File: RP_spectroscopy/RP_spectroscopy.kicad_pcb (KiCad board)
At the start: 2 copper layers, 90.5 x 109 mm, 79 parts, among them J1 Extension connector 1, J10 Conn_Coaxial, J2 Extension connector 2, J3 Conn_Coaxial, J4 Conn_Coaxial, J5 Conn_Coaxial, J6 Conn_Coaxial, J7 Molex PicoBlade, J8 Molex PicoBlade, J9 Conn_Coaxial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

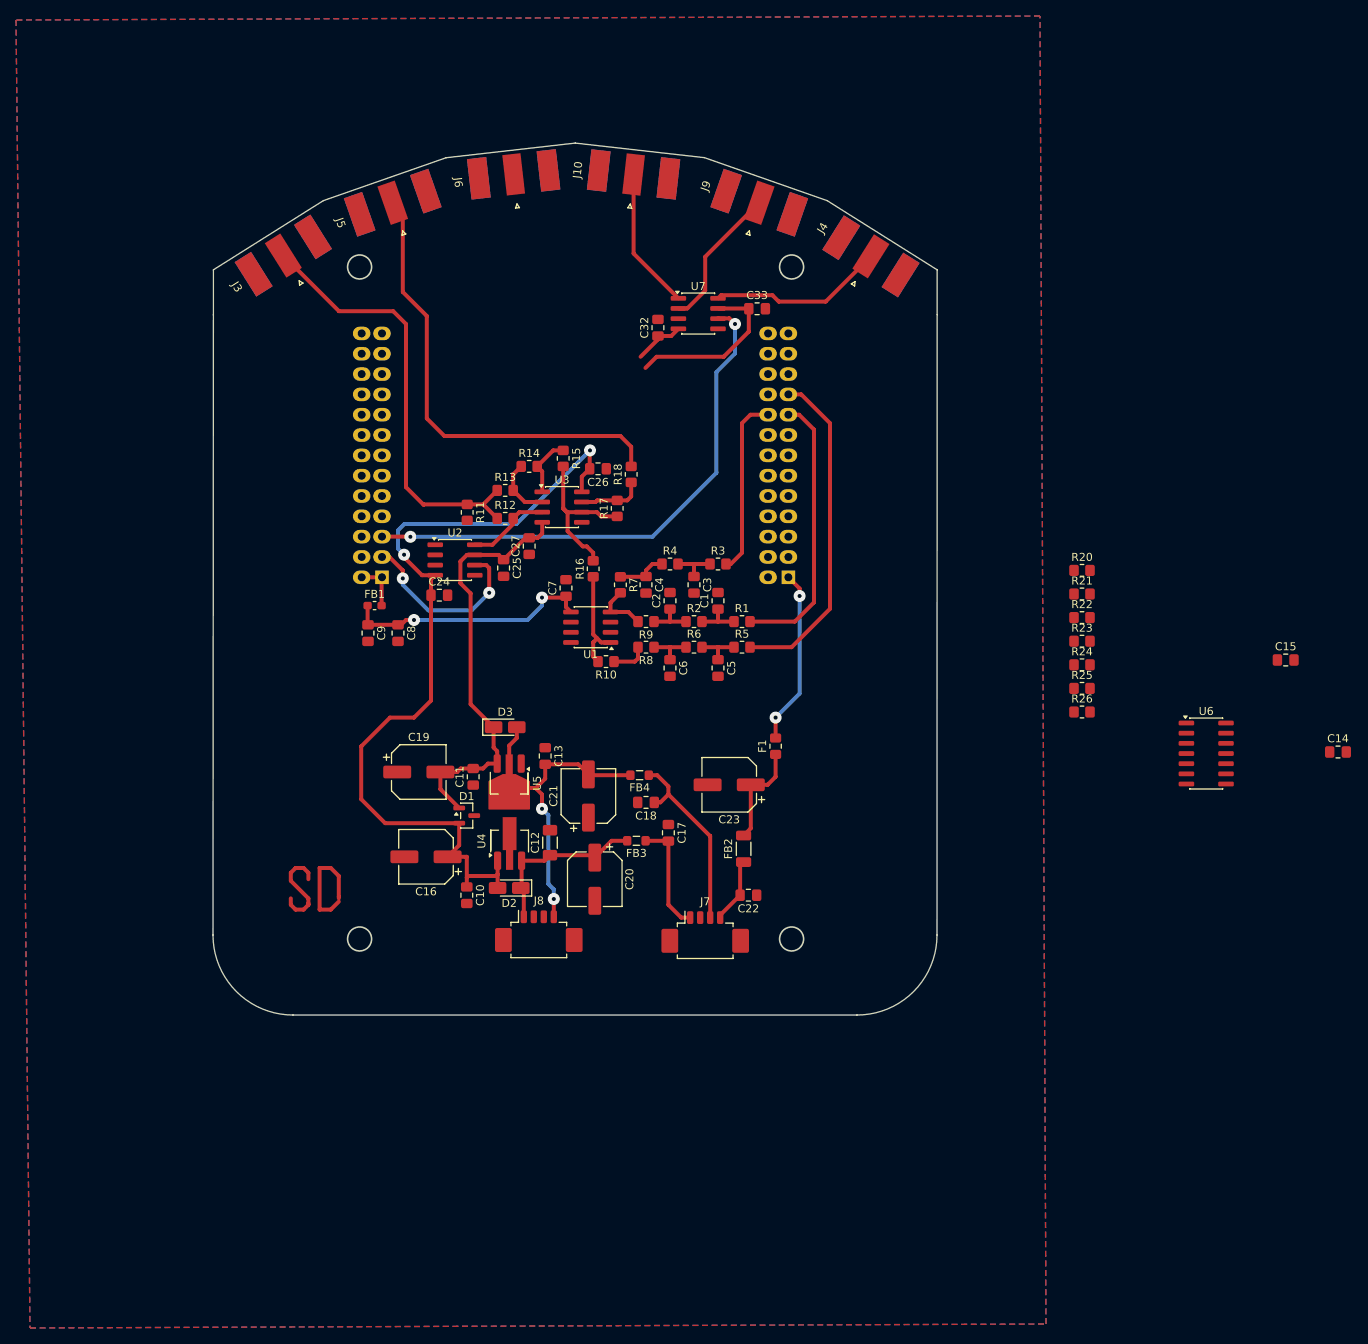
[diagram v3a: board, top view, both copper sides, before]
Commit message: Added the BP filter and the amplification stages. It should be done.
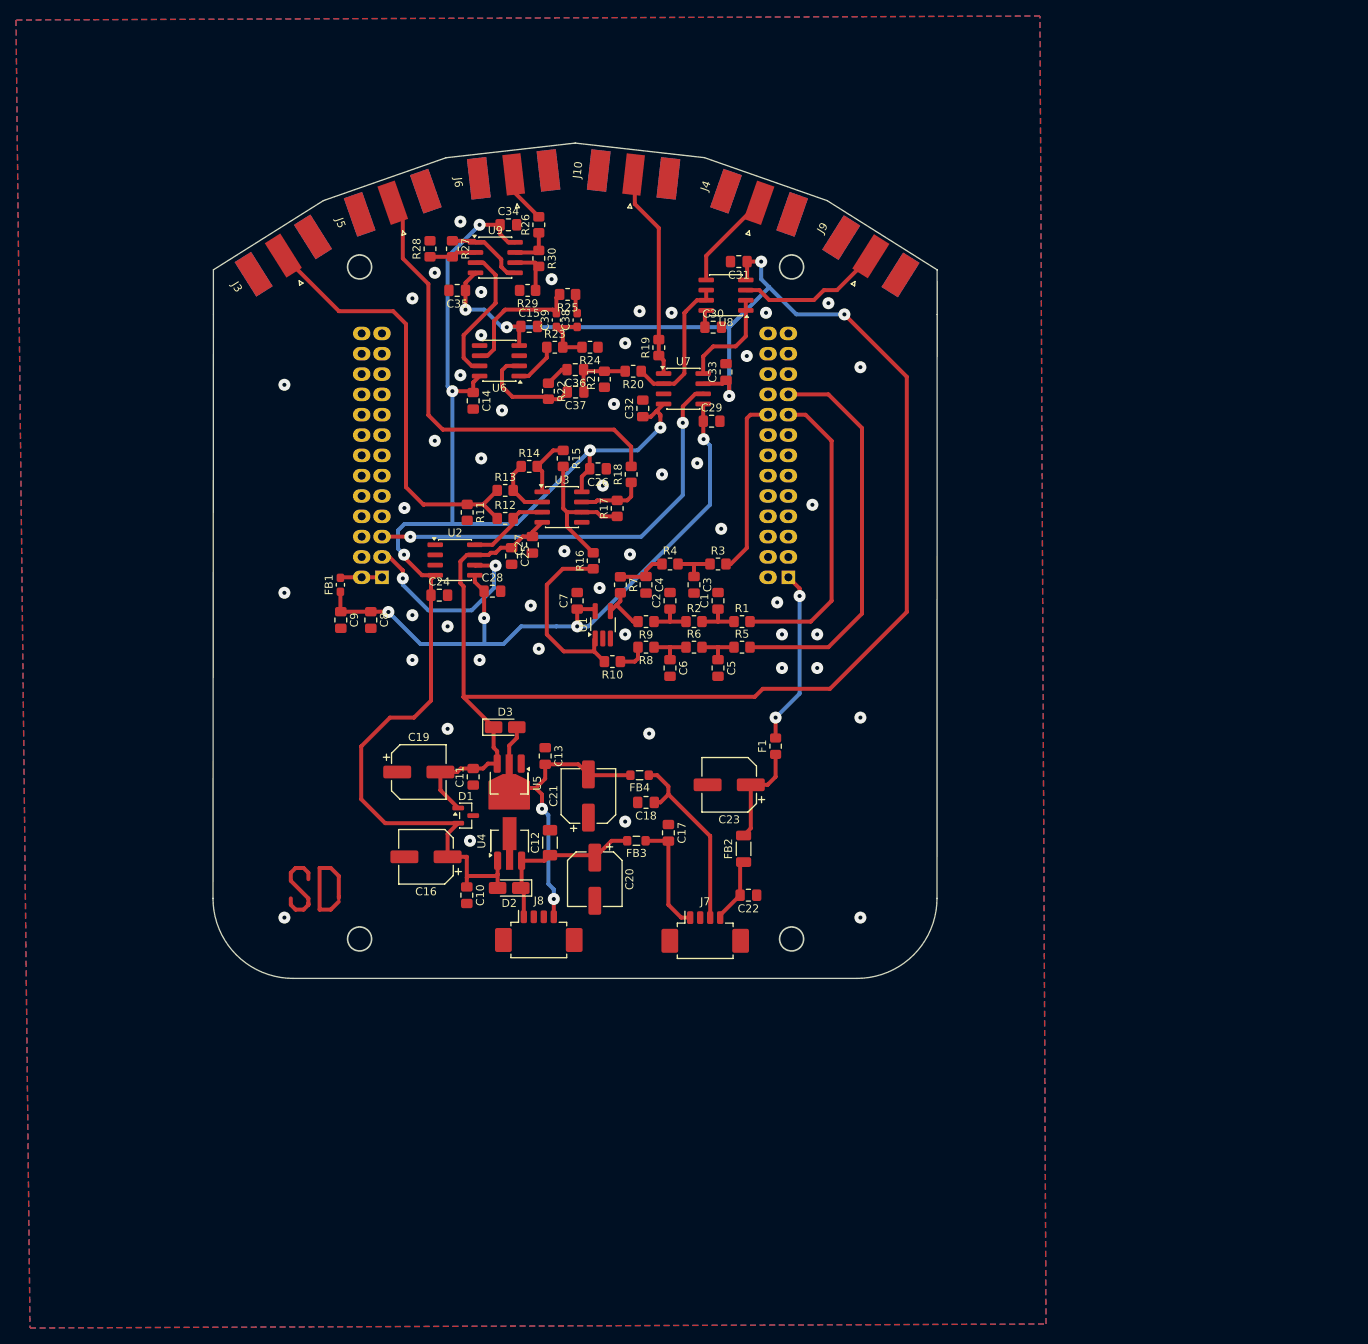
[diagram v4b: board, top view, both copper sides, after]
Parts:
- added C28: 100n, Capacitor_SMD:C_0805_2012Metric_Pad1.18x1.45mm_HandSolder, F.Cu at (124.8, 89.4)
- added C29: 100n, Capacitor_SMD:C_0805_2012Metric_Pad1.18x1.45mm_HandSolder, F.Cu at (152.2, 68.2)
- added C30: 100n, Capacitor_SMD:C_0805_2012Metric_Pad1.18x1.45mm_HandSolder, F.Cu at (152.4, 56.4)
- added C31: 100n, Capacitor_SMD:C_0805_2012Metric_Pad1.18x1.45mm_HandSolder, F.Cu at (155.6, 48.2)
- added C34: 100n, Capacitor_SMD:C_0805_2012Metric_Pad1.18x1.45mm_HandSolder, F.Cu at (126.8, 43.6)
- added C35: 100n, Capacitor_SMD:C_0805_2012Metric_Pad1.18x1.45mm_HandSolder, F.Cu at (120.4, 51.8)
- added C36: 4.3nF, Capacitor_SMD:C_0805_2012Metric_Pad1.18x1.45mm_HandSolder, F.Cu at (135.2, 61.7)
- added C37: 4.3nF, Capacitor_SMD:C_0805_2012Metric_Pad1.18x1.45mm_HandSolder, F.Cu at (135.2, 64.5)
- added C38: 2.4nF, Capacitor_SMD:C_0603_1608Metric_Pad1.08x0.95mm_HandSolder, F.Cu at (135.4, 55.5)
- added C39: 2.4nF, Capacitor_SMD:C_0603_1608Metric_Pad1.08x0.95mm_HandSolder, F.Cu at (132.8, 55.5)
- added R19: 49R9, Resistor_SMD:R_0805_2012Metric_Pad1.20x1.40mm_HandSolder, F.Cu at (145.6, 59.0)
- added R27: R, Resistor_SMD:R_0805_2012Metric_Pad1.20x1.40mm_HandSolder, F.Cu at (119.8, 46.6)
- added R28: R, Resistor_SMD:R_0805_2012Metric_Pad1.20x1.40mm_HandSolder, F.Cu at (117.0, 46.6)
- added R29: R, Resistor_SMD:R_0805_2012Metric_Pad1.20x1.40mm_HandSolder, F.Cu at (129.2, 51.8)
- added R30: R, Resistor_SMD:R_0805_2012Metric_Pad1.20x1.40mm_HandSolder, F.Cu at (130.6, 47.8)
- added U8: LT6231, Package_SO:SOIC-8_3.9x4.9mm_P1.27mm, F.Cu at (154.0, 52.4)
- added U9: LT6231, Package_SO:SOIC-8_3.9x4.9mm_P1.27mm, F.Cu at (125.2, 47.7)
- C14, C15: value 10n -> 100n
- R20: value 5K36 -> 698R
- R21: value 5K36 -> 442R
- R22: value 1k -> 3k65
- R23: value 7K32 -> 698R
- R24: value 1k -> 442R
- R25: value 7K32 -> 3k65
- U1: footprint Package_SO:SOIC-8_3.9x4.9mm_P1.27mm -> Package_TO_SOT_SMD:TSOT-23-5_HandSoldering
- U2: value ADG417BR -> DG418DY-E3
- U6: value OPA1644 -> LT6231; footprint Package_SO:SOIC-14_3.9x8.7mm_P1.27mm -> Package_SO:SOIC-8_3.9x4.9mm_P1.27mm
- moved C14 116.7 mm to (122.4, 65.6), turned to -90 degrees
- moved C15 103.3 mm to (129.4, 56.3)
- moved U6 101.1 mm to (125.7, 60.6), turned to 180 degrees
- moved R26 91.2 mm to (130.6, 43.6), turned to 90 degrees
- moved R25 81.0 mm to (134.2, 52.3), turned to 180 degrees
- moved R23 75.5 mm to (132.6, 58.9)
- moved R24 73.2 mm to (137.0, 58.9), turned to 180 degrees
- moved R22 72.5 mm to (131.8, 64.4), turned to -90 degrees
- moved R21 65.5 mm to (138.8, 62.9), turned to 90 degrees
- moved R20 61.4 mm to (142.4, 61.9), turned to 180 degrees
- moved J4 15.1 mm to (157.6, 42.5), turned to -109.303 degrees
- moved J9 15.1 mm to (171.2, 49.0), turned to -122.169 degrees
- moved C32 10.3 mm to (143.6, 66.5)
- moved U7 9.58 mm to (148.7, 64.1)
- moved C33 8.81 mm to (154.0, 62.0), turned to 90 degrees
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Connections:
- C14 pad 1: PD -> +5VA
- C14 pad 2: Net-(C14-Pad2) -> GND
- C15 pad 1: Net-(C14-Pad2) -> -5VA
- C15 pad 2: Net-(U6A-+) -> GND
- R20 pad 1: Net-(C14-Pad2) -> Buff. diff. PD
- R20 pad 2: Net-(U6A--) -> Net-(C36-Pad1)
- R21 pad 1: Net-(U6A-+) -> GND
- R21 pad 2: GND -> Net-(C36-Pad1)
- R22 pad 1: Net-(U6B--) -> Net-(C36-Pad2)
- R22 pad 2: GND -> Net-(U6A--)
- R23 pad 1: Net-(U6B--) -> Net-(R23-Pad1)
- R23 pad 2: Net-(U6C-+) -> Net-(C38-Pad1)
- R24 pad 1: Net-(U6C--) -> GND
- R24 pad 2: GND -> Net-(C38-Pad1)
- R25 pad 1: Net-(U6C--) -> Net-(C38-Pad2)
- R25 pad 2: Net-(R25-Pad2) -> Net-(U6B--)
- R26 pad 1: Net-(R25-Pad2) -> Net-(R26-Pad1)
- U2 pad 5: unconnected-(U2B-VL-Pad5) -> +3V3
- U6 pad 1: Net-(U6A--) -> Net-(R23-Pad1)
- U6 pad 3: Net-(U6A-+) -> GND
- U6 pad 4: +15V -> -5VA
- U6 pad 5: Net-(U6A--) -> GND
- U6 pad 7: Net-(U6C-+) -> Net-(U9A-+)
- U6 pad 8: Net-(R25-Pad2) -> +5VA
- U7 pad 1: DC PD demultiplexed signal -> Net-(R19-Pad1)
- U7 pad 2: +/- PD -> Buff. diff. PD
- U7 pad 5: unconnected-(U7B-VL-Pad5) -> +3V3
- U7 pad 8: Differential PD -> Net-(U8A--)
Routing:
- net -5VA: track 75.2 -> 235.7 mm, vias 0 -> 5
- net +5VA: track 114.6 -> 176.7 mm, vias 2 -> 5
- net +3V3: track 31.4 -> 84.1 mm, vias 2 -> 4
- net Buff. diff. PD: track 0.00 -> 18.8 mm
- net Net-(U9A-+): track 0.00 -> 17.6 mm
- net Net-(U6B--): track 0.00 -> 16.8 mm
- net Net-(U6A--): track 0.00 -> 13.5 mm
- net Net-(U8A--): track 0.00 -> 13.0 mm
- net Multiplex switch: track 67.1 -> 54.1 mm
- net Net-(U9B-+): track 0.00 -> 10.0 mm
- net Net-(R10-Pad2): track 13.2 -> 22.9 mm
- net Differential PD: track 22.0 -> 12.4 mm
- net Net-(C36-Pad1): track 0.00 -> 8.10 mm
- net Small offset: track 41.9 -> 49.9 mm
- net Net-(C38-Pad1): track 0.00 -> 7.87 mm
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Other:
- board size 90.5 x 109 mm -> 90.5 x 104.4 mm

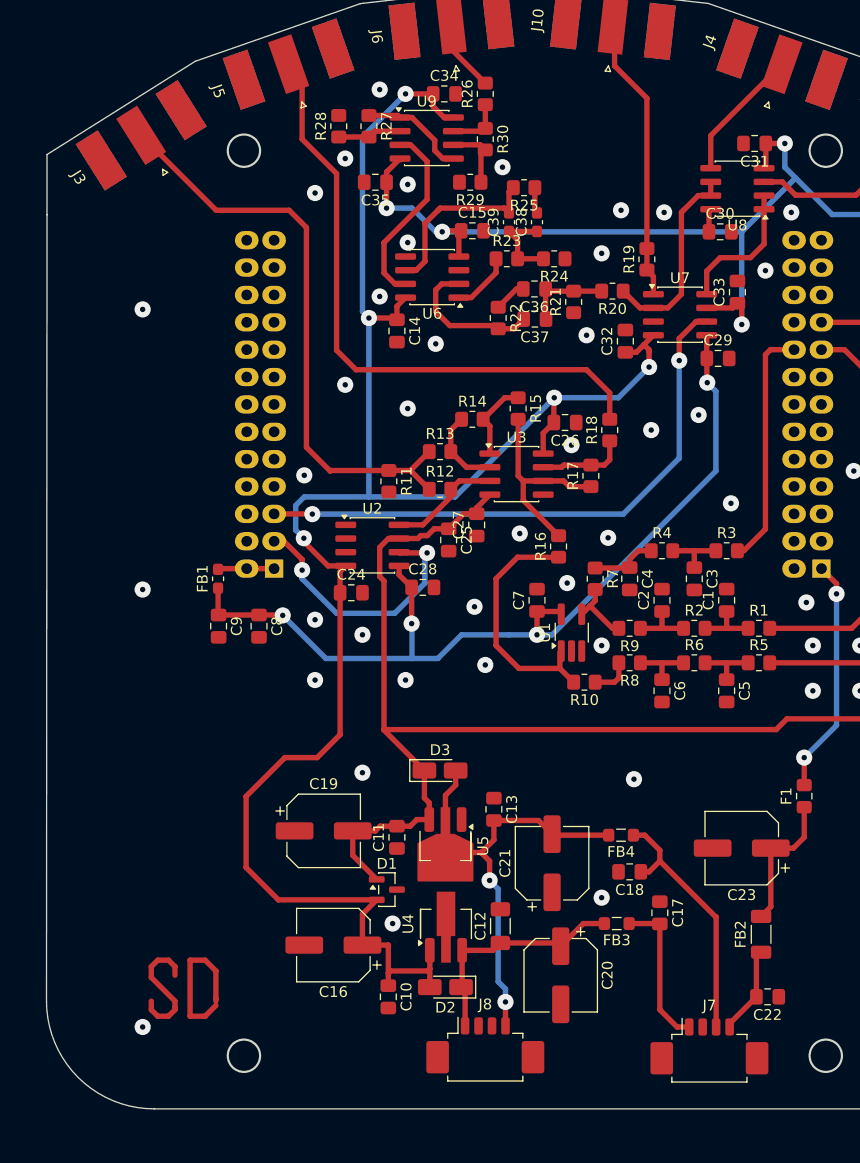
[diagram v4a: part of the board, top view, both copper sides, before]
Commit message: Project modified to solve the routing problems found while soldering
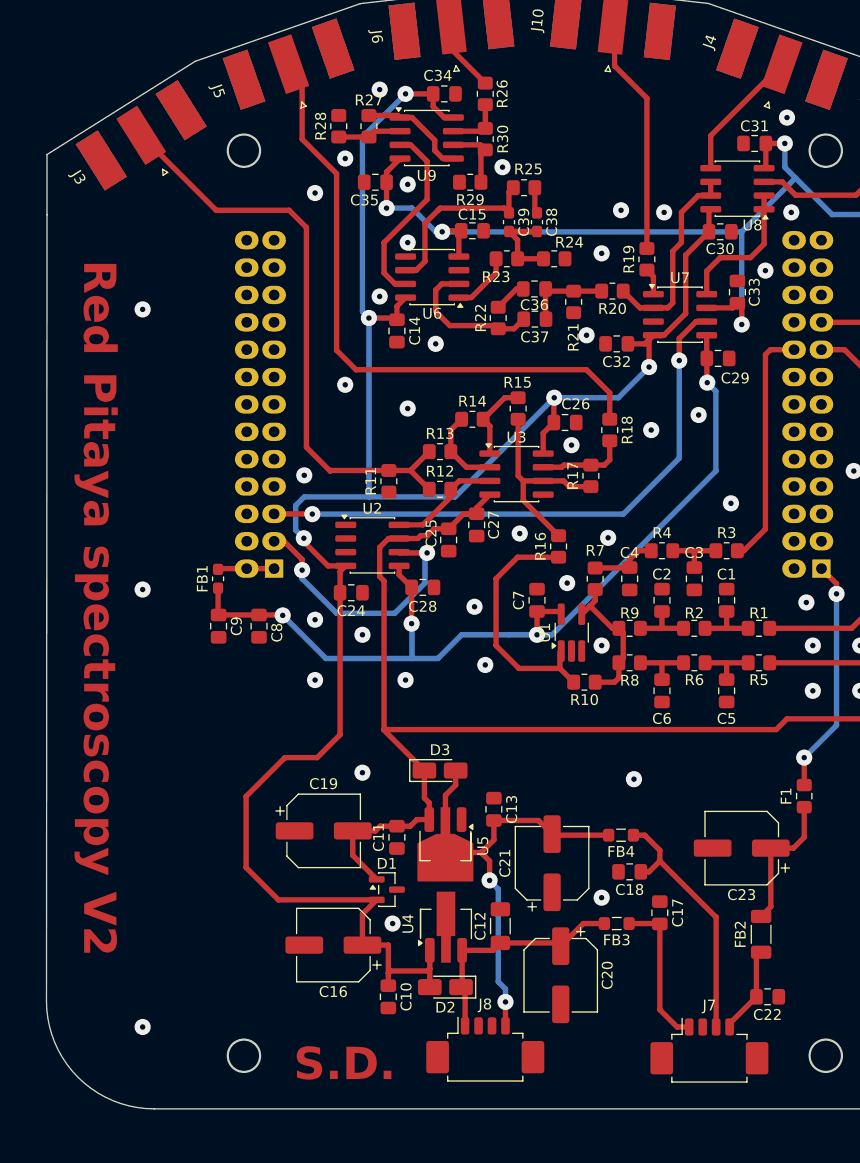
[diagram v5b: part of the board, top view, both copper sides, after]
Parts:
- moved C32 0.84 mm to (142.8, 66.8), turned to 180 degrees
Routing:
- net (no net): track 25.7 -> 0.00 mm
- net +5VA: track 176.7 -> 189.3 mm
- net Net-(U1--): track 10.1 -> 13.6 mm
- net DC PD demultiplexed signal: track 23.6 -> 21.9 mm
- net GND: vias 48 -> 49
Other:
- board text added: "Red Pitaya spectroscopy V2"
- board text added: "S.D."
